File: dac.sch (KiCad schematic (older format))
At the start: 46 parts, among them U15 OPA4172, U4 OPA4172, U8 DAC8568C

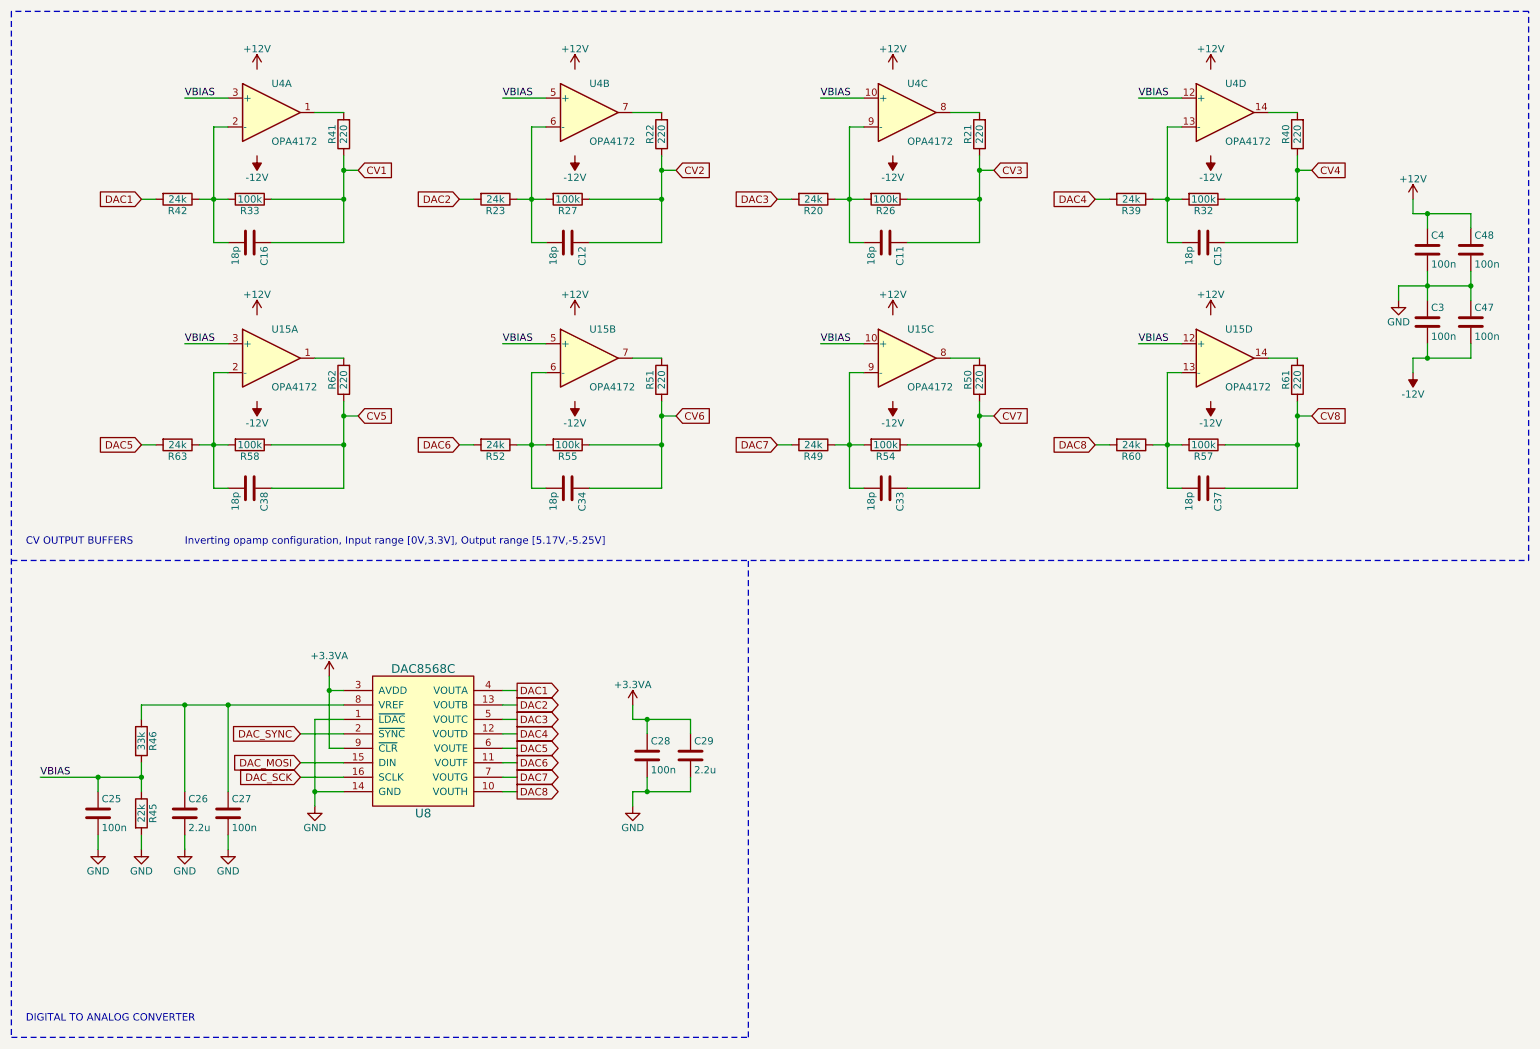
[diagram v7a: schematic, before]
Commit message: renumbered components
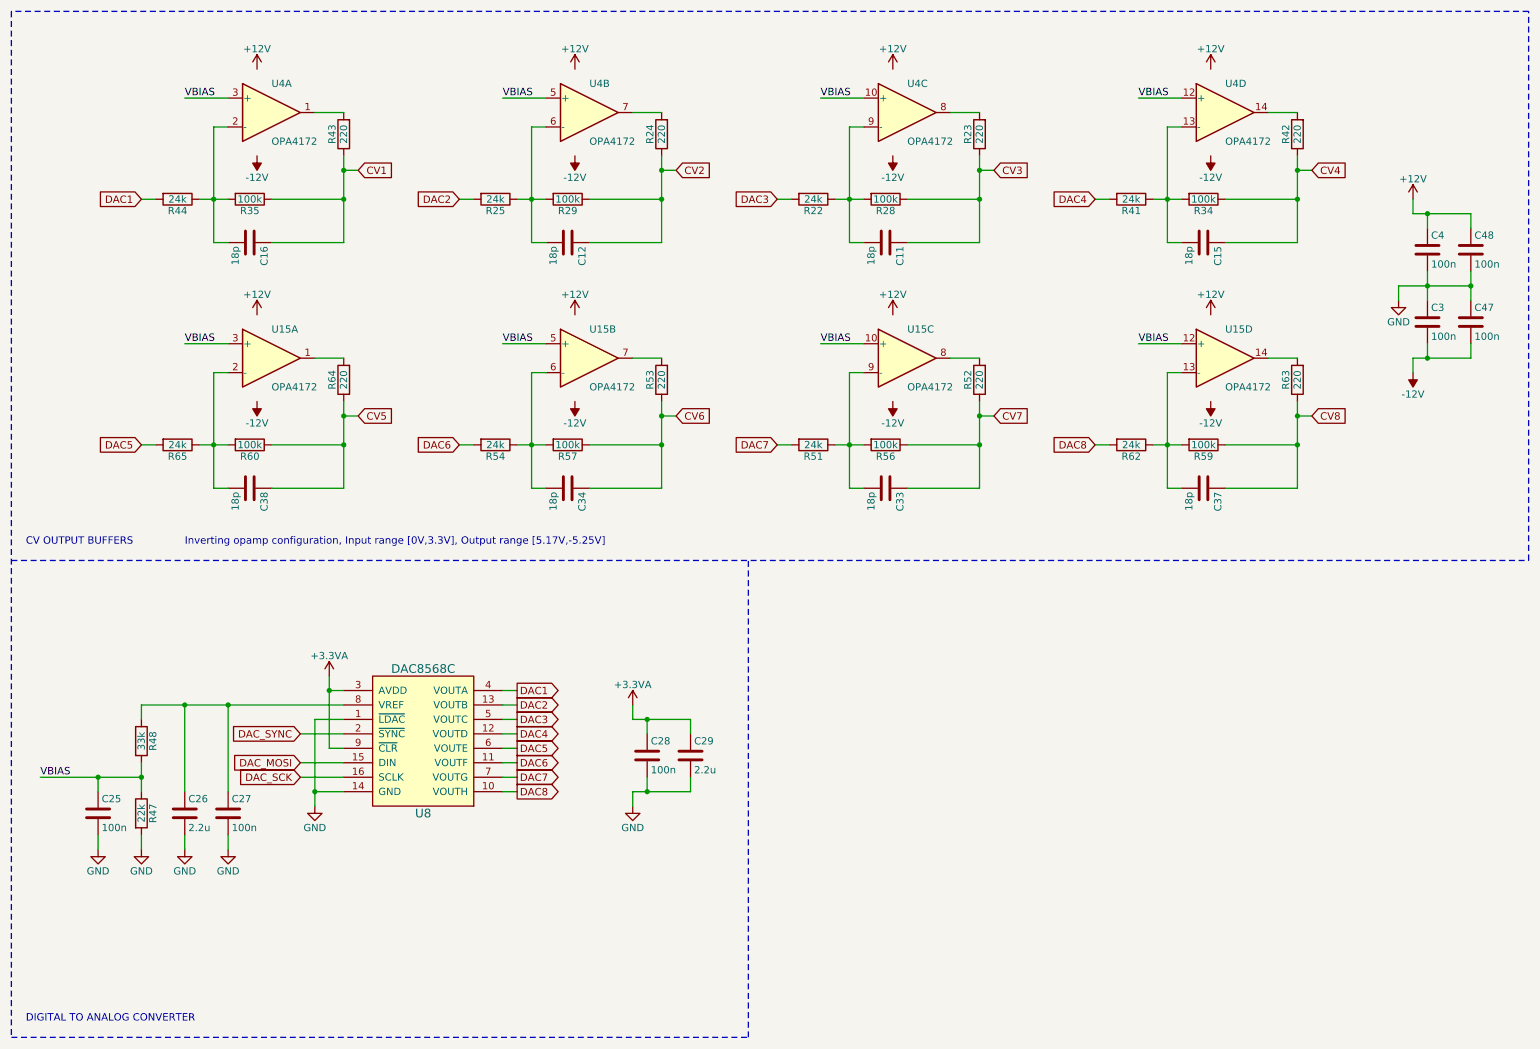
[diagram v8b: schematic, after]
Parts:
- renumbered R20 to R22, R21 to R23, R22 to R24, R23 to R25, R26 to R28, R27 to R29, R32 to R34, R33 to R35, R39 to R41, R40 to R42, R41 to R43, R42 to R44, R45 to R47, R46 to R48, R49 to R51, R50 to R52, R51 to R53, R52 to R54, R54 to R56, R55 to R57, R57 to R59, R58 to R60, R60 to R62, R61 to R63, R62 to R64, R63 to R65
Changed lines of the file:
@@
 $EndComp
 $Comp
-L R R33
+L R R35
 U 1 1 59E36D15
 P 2250 1900
-F 0 "R33" V 2330 1900 50  0000 C CNN
+F 0 "R35" V 2330 1900 50  0000 C CNN
 F 1 "100k" V 2250 1900 50  0000 C CNN
 F 2 "w_resistor:R_0603" V 2180 1900 50  0001 C CNN
@@
 $EndComp
 $Comp
-L R R42
+L R R44
 U 1 1 59E36D6E
 P 1750 1900
-F 0 "R42" V 1830 1900 50  0000 C CNN
+F 0 "R44" V 1830 1900 50  0000 C CNN
 F 1 "24k" V 1750 1900 50  0000 C CNN
 F 2 "w_resistor:R_0603" V 1680 1900 50  0001 C CNN
@@
 $EndComp
 $Comp
-L R R41
+L R R43
 U 1 1 59E36DB8
 P 2900 1450
-F 0 "R41" V 2980 1450 50  0000 C CNN
+F 0 "R43" V 2980 1450 50  0000 C CNN
 F 1 "220" V 2900 1450 50  0000 C CNN
 F 2 "w_resistor:R_0603" V 2830 1450 50  0001 C CNN
@@
 $EndComp
 $Comp
-L R R27
+L R R29
 U 1 1 59E399B0
 P 4450 1900
-F 0 "R27" V 4530 1900 50  0000 C CNN
+F 0 "R29" V 4530 1900 50  0000 C CNN
 F 1 "100k" V 4450 1900 50  0000 C CNN
 F 2 "w_resistor:R_0603" V 4380 1900 50  0001 C CNN
@@
 $EndComp
 $Comp
-L R R23
+L R R25
 U 1 1 59E399B8
 P 3950 1900
-F 0 "R23" V 4030 1900 50  0000 C CNN
+F 0 "R25" V 4030 1900 50  0000 C CNN
 F 1 "24k" V 3950 1900 50  0000 C CNN
 F 2 "w_resistor:R_0603" V 3880 1900 50  0001 C CNN
@@
 $EndComp
 $Comp
-L R R22
+L R R24
 U 1 1 59E399C0
 P 5100 1450
-F 0 "R22" V 5180 1450 50  0000 C CNN
+F 0 "R24" V 5180 1450 50  0000 C CNN
 F 1 "220" V 5100 1450 50  0000 C CNN
 F 2 "w_resistor:R_0603" V 5030 1450 50  0001 C CNN
@@
 $EndComp
 $Comp
-L R R26
+L R R28
 U 1 1 59E39C95
 P 6650 1900
-F 0 "R26" V 6730 1900 50  0000 C CNN
+F 0 "R28" V 6730 1900 50  0000 C CNN
 F 1 "100k" V 6650 1900 50  0000 C CNN
 F 2 "w_resistor:R_0603" V 6580 1900 50  0001 C CNN
@@
 $EndComp
 $Comp
-L R R20
+L R R22
 U 1 1 59E39C9D
 P 6150 1900
-F 0 "R20" V 6230 1900 50  0000 C CNN
+F 0 "R22" V 6230 1900 50  0000 C CNN
 F 1 "24k" V 6150 1900 50  0000 C CNN
 F 2 "w_resistor:R_0603" V 6080 1900 50  0001 C CNN
@@
 $EndComp
 $Comp
-L R R21
+L R R23
 U 1 1 59E39CA5
 P 7300 1450
-F 0 "R21" V 7380 1450 50  0000 C CNN
+F 0 "R23" V 7380 1450 50  0000 C CNN
 F 1 "220" V 7300 1450 50  0000 C CNN
 F 2 "w_resistor:R_0603" V 7230 1450 50  0001 C CNN
@@
 $EndComp
 $Comp
-L R R32
+L R R34
 U 1 1 59E39CDE
 P 8850 1900
-F 0 "R32" V 8930 1900 50  0000 C CNN
+F 0 "R34" V 8930 1900 50  0000 C CNN
 F 1 "100k" V 8850 1900 50  0000 C CNN
 F 2 "w_resistor:R_0603" V 8780 1900 50  0001 C CNN
@@
 $EndComp
 $Comp
-L R R39
+L R R41
 U 1 1 59E39CE6
 P 8350 1900
-F 0 "R39" V 8430 1900 50  0000 C CNN
+F 0 "R41" V 8430 1900 50  0000 C CNN
 F 1 "24k" V 8350 1900 50  0000 C CNN
 F 2 "w_resistor:R_0603" V 8280 1900 50  0001 C CNN
@@
 $EndComp
 $Comp
-L R R40
+L R R42
 U 1 1 59E39CEE
 P 9500 1450
-F 0 "R40" V 9580 1450 50  0000 C CNN
+F 0 "R42" V 9580 1450 50  0000 C CNN
 F 1 "220" V 9500 1450 50  0000 C CNN
 F 2 "w_resistor:R_0603" V 9430 1450 50  0001 C CNN
@@
 $EndComp
 $Comp
-L R R58
+L R R60
 U 1 1 59E3B2A4
 P 2250 3600
-F 0 "R58" V 2330 3600 50  0000 C CNN
+F 0 "R60" V 2330 3600 50  0000 C CNN
 F 1 "100k" V 2250 3600 50  0000 C CNN
 F 2 "w_resistor:R_0603" V 2180 3600 50  0001 C CNN
@@
 $EndComp
 $Comp
-L R R63
+L R R65
 U 1 1 59E3B2AC
 P 1750 3600
-F 0 "R63" V 1830 3600 50  0000 C CNN
+F 0 "R65" V 1830 3600 50  0000 C CNN
 F 1 "24k" V 1750 3600 50  0000 C CNN
 F 2 "w_resistor:R_0603" V 1680 3600 50  0001 C CNN
@@
 $EndComp
 $Comp
-L R R62
+L R R64
 U 1 1 59E3B2B4
 P 2900 3150
-F 0 "R62" V 2980 3150 50  0000 C CNN
+F 0 "R64" V 2980 3150 50  0000 C CNN
 F 1 "220" V 2900 3150 50  0000 C CNN
 F 2 "w_resistor:R_0603" V 2830 3150 50  0001 C CNN
@@
 $EndComp
 $Comp
-L R R55
+L R R57
 U 1 1 59E3B2E9
 P 4450 3600
-F 0 "R55" V 4530 3600 50  0000 C CNN
+F 0 "R57" V 4530 3600 50  0000 C CNN
 F 1 "100k" V 4450 3600 50  0000 C CNN
 F 2 "w_resistor:R_0603" V 4380 3600 50  0001 C CNN
@@
 $EndComp
 $Comp
-L R R52
+L R R54
 U 1 1 59E3B2F1
 P 3950 3600
-F 0 "R52" V 4030 3600 50  0000 C CNN
+F 0 "R54" V 4030 3600 50  0000 C CNN
 F 1 "24k" V 3950 3600 50  0000 C CNN
 F 2 "w_resistor:R_0603" V 3880 3600 50  0001 C CNN
@@
 $EndComp
 $Comp
-L R R51
+L R R53
 U 1 1 59E3B2F9
 P 5100 3150
-F 0 "R51" V 5180 3150 50  0000 C CNN
+F 0 "R53" V 5180 3150 50  0000 C CNN
 F 1 "220" V 5100 3150 50  0000 C CNN
 F 2 "w_resistor:R_0603" V 5030 3150 50  0001 C CNN
@@
 $EndComp
 $Comp
-L R R54
+L R R56
 U 1 1 59E3B32E
 P 6650 3600
-F 0 "R54" V 6730 3600 50  0000 C CNN
+F 0 "R56" V 6730 3600 50  0000 C CNN
 F 1 "100k" V 6650 3600 50  0000 C CNN
 F 2 "w_resistor:R_0603" V 6580 3600 50  0001 C CNN
@@
 $EndComp
 $Comp
-L R R49
+L R R51
 U 1 1 59E3B336
 P 6150 3600
-F 0 "R49" V 6230 3600 50  0000 C CNN
+F 0 "R51" V 6230 3600 50  0000 C CNN
 F 1 "24k" V 6150 3600 50  0000 C CNN
 F 2 "w_resistor:R_0603" V 6080 3600 50  0001 C CNN
@@
 $EndComp
 $Comp
-L R R50
+L R R52
 U 1 1 59E3B33E
 P 7300 3150
-F 0 "R50" V 7380 3150 50  0000 C CNN
+F 0 "R52" V 7380 3150 50  0000 C CNN
 F 1 "220" V 7300 3150 50  0000 C CNN
 F 2 "w_resistor:R_0603" V 7230 3150 50  0001 C CNN
@@
 $EndComp
 $Comp
-L R R57
+L R R59
 U 1 1 59E3B373
 P 8850 3600
-F 0 "R57" V 8930 3600 50  0000 C CNN
+F 0 "R59" V 8930 3600 50  0000 C CNN
 F 1 "100k" V 8850 3600 50  0000 C CNN
 F 2 "w_resistor:R_0603" V 8780 3600 50  0001 C CNN
@@
 $EndComp
 $Comp
-L R R60
+L R R62
 U 1 1 59E3B37B
 P 8350 3600
-F 0 "R60" V 8430 3600 50  0000 C CNN
+F 0 "R62" V 8430 3600 50  0000 C CNN
 F 1 "24k" V 8350 3600 50  0000 C CNN
 F 2 "w_resistor:R_0603" V 8280 3600 50  0001 C CNN
@@
 $EndComp
 $Comp
-L R R61
+L R R63
 U 1 1 59E3B383
 P 9500 3150
-F 0 "R61" V 9580 3150 50  0000 C CNN
+F 0 "R63" V 9580 3150 50  0000 C CNN
 F 1 "220" V 9500 3150 50  0000 C CNN
 F 2 "w_resistor:R_0603" V 9430 3150 50  0001 C CNN
@@
 $EndComp
 $Comp
-L R R46
+L R R48
 U 1 1 59F015C8
 P 1500 5650
-F 0 "R46" V 1580 5650 50  0000 C CNN
+F 0 "R48" V 1580 5650 50  0000 C CNN
 F 1 "33k" V 1500 5650 50  0000 C CNN
 F 2 "w_resistor:R_0603" V 1430 5650 50  0001 C CNN
@@
 $EndComp
 $Comp
-L R R45
+L R R47
 U 1 1 59F01689
 P 1500 6150
-F 0 "R45" V 1580 6150 50  0000 C CNN
+F 0 "R47" V 1580 6150 50  0000 C CNN
 F 1 "22k" V 1500 6150 50  0000 C CNN
 F 2 "w_resistor:R_0603" V 1430 6150 50  0001 C CNN
